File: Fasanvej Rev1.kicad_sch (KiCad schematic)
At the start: 43 parts

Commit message: Finalized schematics some more. Still missing a few footprints.
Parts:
- removed J?: AudioJack3, Connector_Audio:Jack_3.5mm_CUI_SJ-3523-SMT_Horizontal, symbol Connector:AudioJack3
- removed J?: USB_A, symbol Connector:USB_A
- removed LS?: Soberton SP-1609-2, Connector_PinHeader_2.54mm:PinHeader_1x02_P2.54mm_Vertical, symbol Device:Speaker
- removed RV?: 1k, symbol Device:R_Potentiometer_Dual
- removed SW?: SW_DPDT_x2, symbol Switch:SW_DPDT_x2
- removed SW?: SW_DPDT_x2, Button_Switch_THT:SW_E-Switch_EG2219_DPDT_Angled, symbol Switch:SW_DPDT_x2
- added FID1, FID2: Fiducial, Fiducial:Fiducial_1.5mm_Mask3mm, symbol Mechanical:Fiducial
- added H1, H2, H3, H4, H5, H6, H7, H8: M3, MountingHole:MountingHole_3.2mm_M3, symbol Mechanical:MountingHole
- added J1, J2: Molex 676430910, RISRES Library:USB_A_Molex_67643_Horizontal, symbol Connector:USB_A
- added J5: UART console, Connector_PinHeader_2.54mm:PinHeader_1x04_P2.54mm_Vertical, symbol Connector_Generic:Conn_01x04
- J3: renamed from J?; footprint (none) -> RISRES Library:TE_4-1734839-0_1x40-1MP_P0.5mm_Horizontal
- SW1: renamed from SW?; value SW_Push -> TL3342F260QG; footprint (none) -> Button_Switch_SMD:SW_SPST_TL3342
- Y1: renamed from Y?; footprint (none) -> Crystal:Crystal_SMD_HC49-SD_HandSoldering
- gave numbers to parts that had none: 34
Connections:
- net SPK_LEFT is gone; now on net HP_L: LS1.2
- net +3V3: now also J5.1 (Pin_1)
- net GND: now also J1.4 (GND), J1.5 (Shield), J2.4 (GND), J5.4 (Pin_4)
- net UART_RX: now also J5.2 (Pin_2)
- net UART_TX: now also J5.3 (Pin_3)
- net USB_DM_WIFI: now also J1.2 (D-)
- net USB_DP_WIFI: now also J1.3 (D+)
- net USB_VBUS_EXTERNAL: now also J2.1 (VBUS)
- net at C4.2, R4.1, U2.2 (GND): now also J2.5 (Shield)
- net at U2.4 (I/O2): now also J2.3 (D+)
- net at U2.6 (I/O1): now also J2.2 (D-)
- new net +5V: J1.1 (VBUS)
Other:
- moved on the sheet: C10, C11, C12, C13, C14, C15, C16, C17, C18, C7, C8, C9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

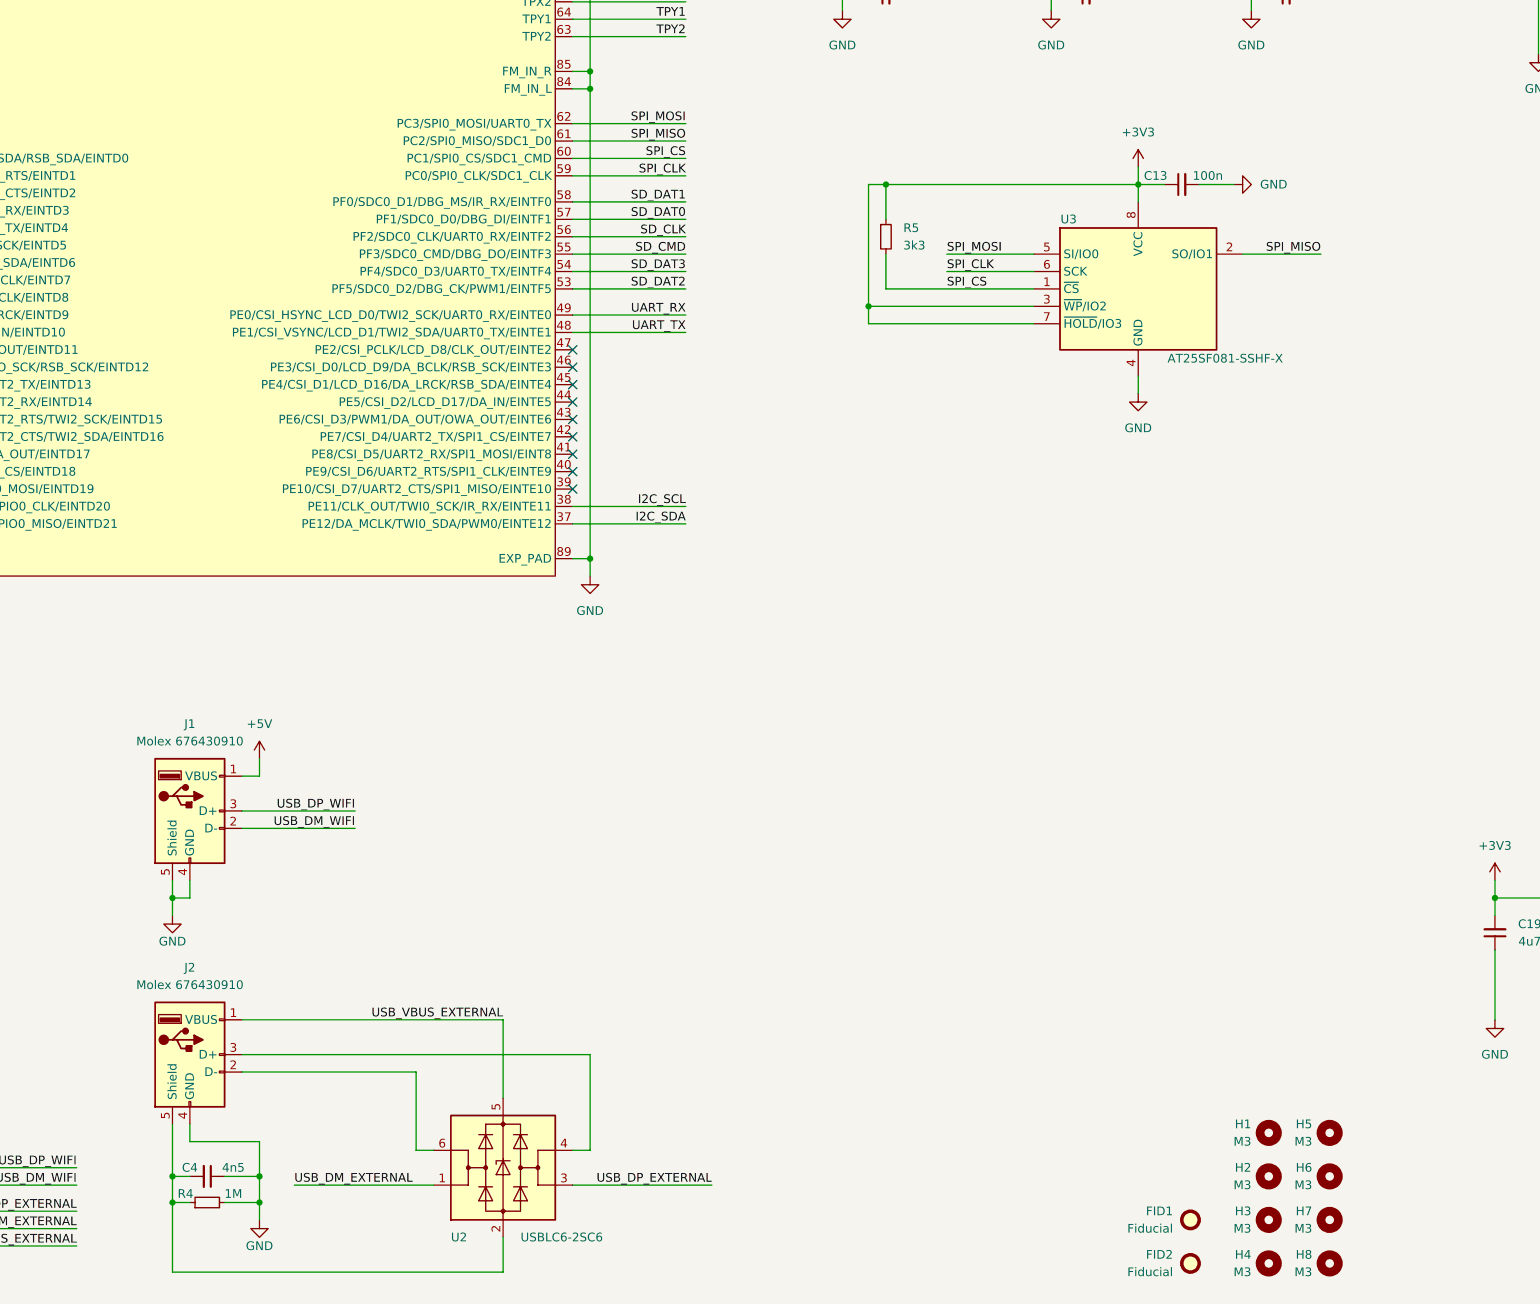
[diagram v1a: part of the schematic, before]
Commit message: Schematic finalized. Started PCB layout.
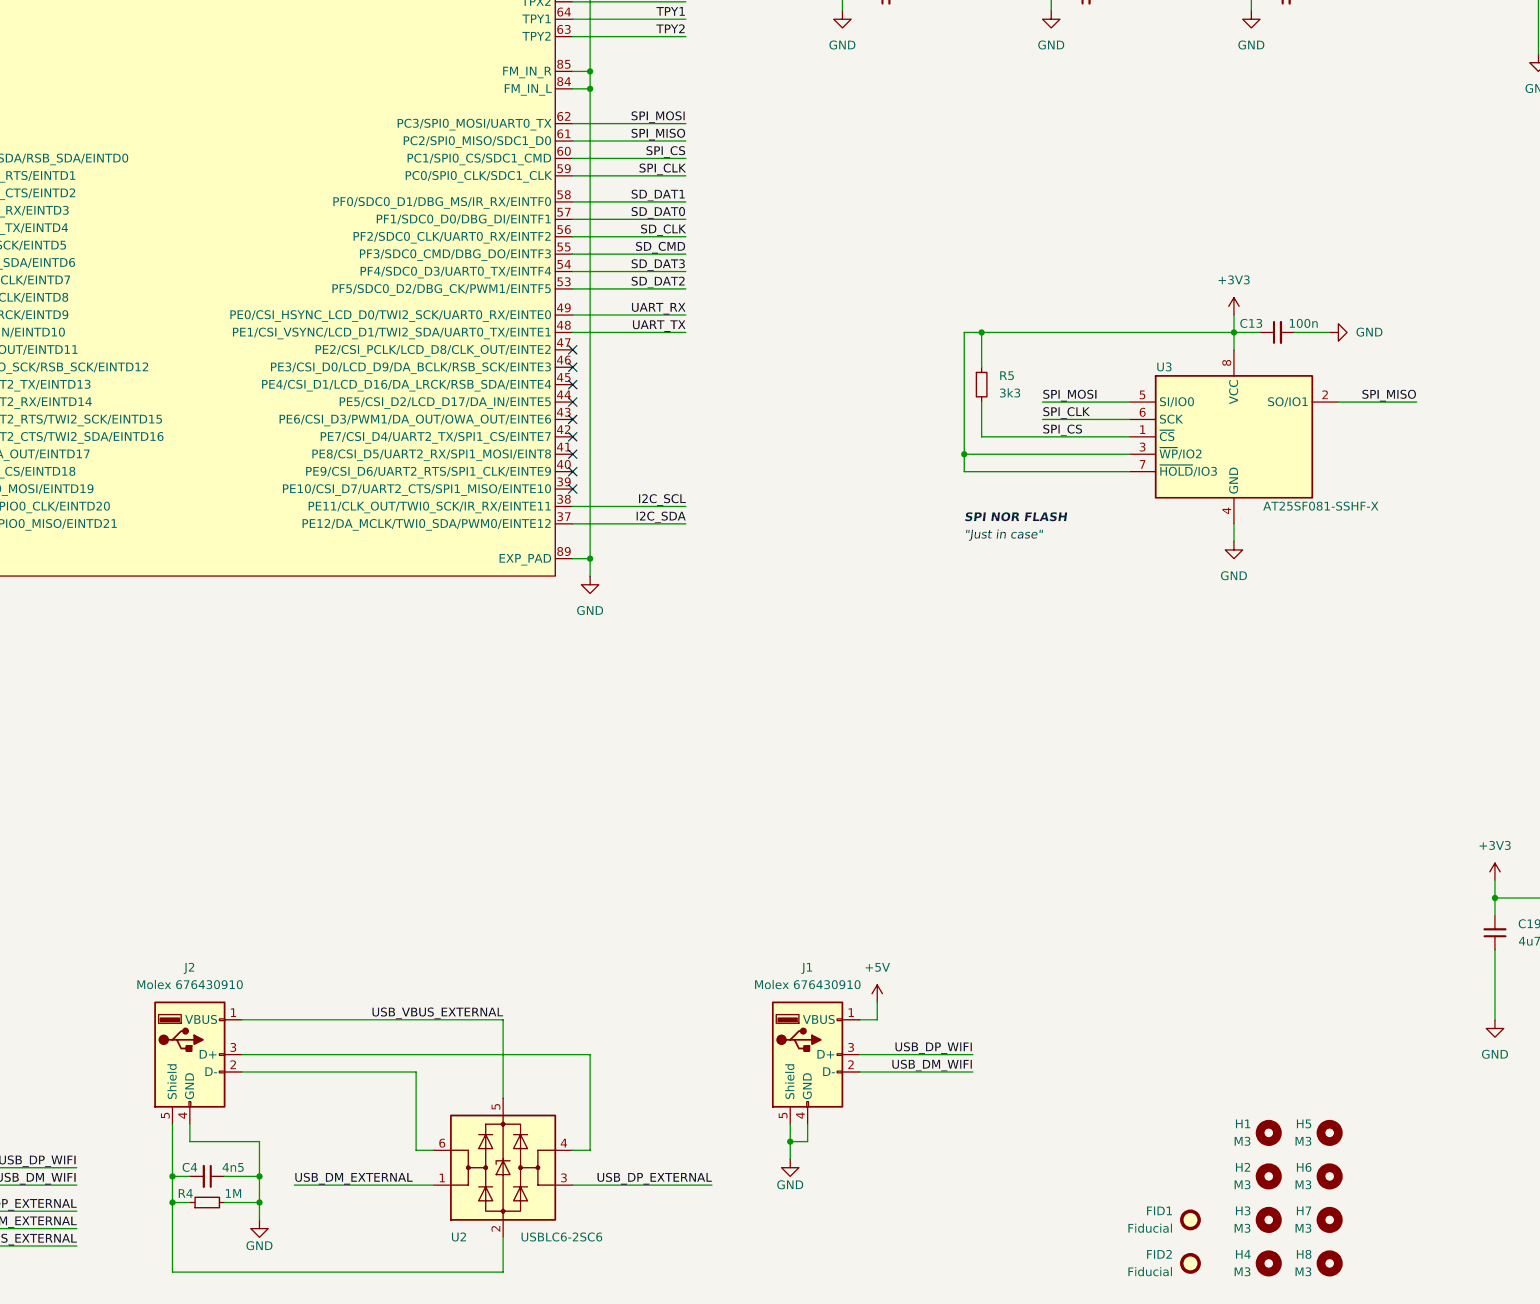
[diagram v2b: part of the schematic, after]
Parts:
- J4: footprint (none) -> Connector_Card:microSD_HC_Hirose_DM3D-SF
- U1: footprint (none) -> RISRES Library:QFN-88_EP_10x10_Pitch0.4mm
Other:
- note added: ""Just in case""
- note added: "SPI NOR FLASH"
- moved on the sheet: C13, J1, R5, U3

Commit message: Made a lot of progress laying out PCB
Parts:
- removed J3: LCD_RGB_40P, RISRES Library:TE_4-1734839-0_1x40-1MP_P0.5mm_Horizontal, symbol RISRES Library:LCD_RGB_40P
- removed TP2, TP3: TestPoint_Small, TestPoint:TestPoint_Pad_D4.0mm, symbol Connector:TestPoint_Small
- added J13: I2C keyboard, Connector_PinHeader_2.54mm:PinHeader_2x02_P2.54mm_Vertical, symbol Connector_Generic:Conn_02x02_Top_Bottom
- added J3: LQ035NC111, RISRES Library:FFC2B22-54-T, symbol Connector_Generic:Conn_02x27_Counter_Clockwise
- added R43, R44: 4k7, Resistor_SMD:R_0603_1608Metric_Pad0.98x0.95mm_HandSolder, symbol Device:R_Small
- added R45: 22k, Resistor_SMD:R_0603_1608Metric_Pad0.98x0.95mm_HandSolder, symbol Device:R_Small
- renumbered J2 to J1, J1 to J2
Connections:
- net +3V3: now also J3.41 (Pin_41), J3.42 (Pin_42), R43.1, R44.1, R45.2
- net GND: now also J3.12 (Pin_12), J3.13 (Pin_13), J3.20 (Pin_20), J3.21 (Pin_21), J3.28 (Pin_28), J3.29 (Pin_29), J3.48 (Pin_48), J3.49 (Pin_49), J3.50 (Pin_50), J3.53 (Pin_53), J3.54 (Pin_54)
- net I2C_SCL: now also J13.1 (Pin_1), R43.2; no longer TP1.1
- net I2C_SDA: now also J13.2 (Pin_2), R44.2
- net LCD_CLK: now also J3.38 (Pin_38)
- net LCD_D10: now also J3.22 (Pin_22)
- net LCD_D11: now also TP1.1, J3.23 (Pin_23)
- net LCD_D12: now also J3.24 (Pin_24)
- net LCD_D13: now also J3.25 (Pin_25)
- net LCD_D14: now also J3.26 (Pin_26)
- net LCD_D15: now also J3.27 (Pin_27)
- net LCD_D18: now also J3.35 (Pin_35)
- net LCD_D19: now also J3.34 (Pin_34)
- net LCD_D2: now also J3.14 (Pin_14)
- net LCD_D20: now also J3.33 (Pin_33)
- net LCD_D21: now also J3.32 (Pin_32)
- net LCD_D22: now also J3.31 (Pin_31)
- net LCD_D23: now also J3.30 (Pin_30)
- net LCD_D3: now also J3.15 (Pin_15)
- net LCD_D4: now also J3.16 (Pin_16)
- net LCD_D5: now also J3.17 (Pin_17)
- net LCD_D6: now also J3.18 (Pin_18)
- net LCD_D7: now also J3.19 (Pin_19)
- net LCD_DE: now also J3.52 (Pin_52)
- net LCD_HSYNC: now also J3.36 (Pin_36)
- net LCD_VSYNC: now also J3.37 (Pin_37)
- net LED_BACKLIGHT_A: now also J3.3 (Pin_3), J3.4 (Pin_4)
- net LED_BACKLIGHT_K: now also J3.1 (Pin_1), J3.2 (Pin_2)
- net USB_DM_EXTERNAL: now also U2.3 (I/O2); no longer U2.1 (I/O1)
- net USB_DP_EXTERNAL: now also U2.1 (I/O1); no longer U2.3 (I/O2)
- net at J1.2 (D-): now also U2.4 (I/O2); no longer U2.6 (I/O1)
- net at J1.3 (D+): now also U2.6 (I/O1); no longer U2.4 (I/O2)
- new net: J3.10 (Pin_10), J3.11 (Pin_11), J3.8 (Pin_8), J3.9 (Pin_9), R45.1
- new net KEYBOARD_S1_P0: J13.3 (Pin_3)
- new net KEYBOARD_S1_P1: J13.4 (Pin_4)
- no-connect marks 17 -> 28
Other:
- sheet Keyboard ports: added SERCOM1_PAD0, SERCOM1_PAD1; removed none
- moved on the sheet: C21, TP1

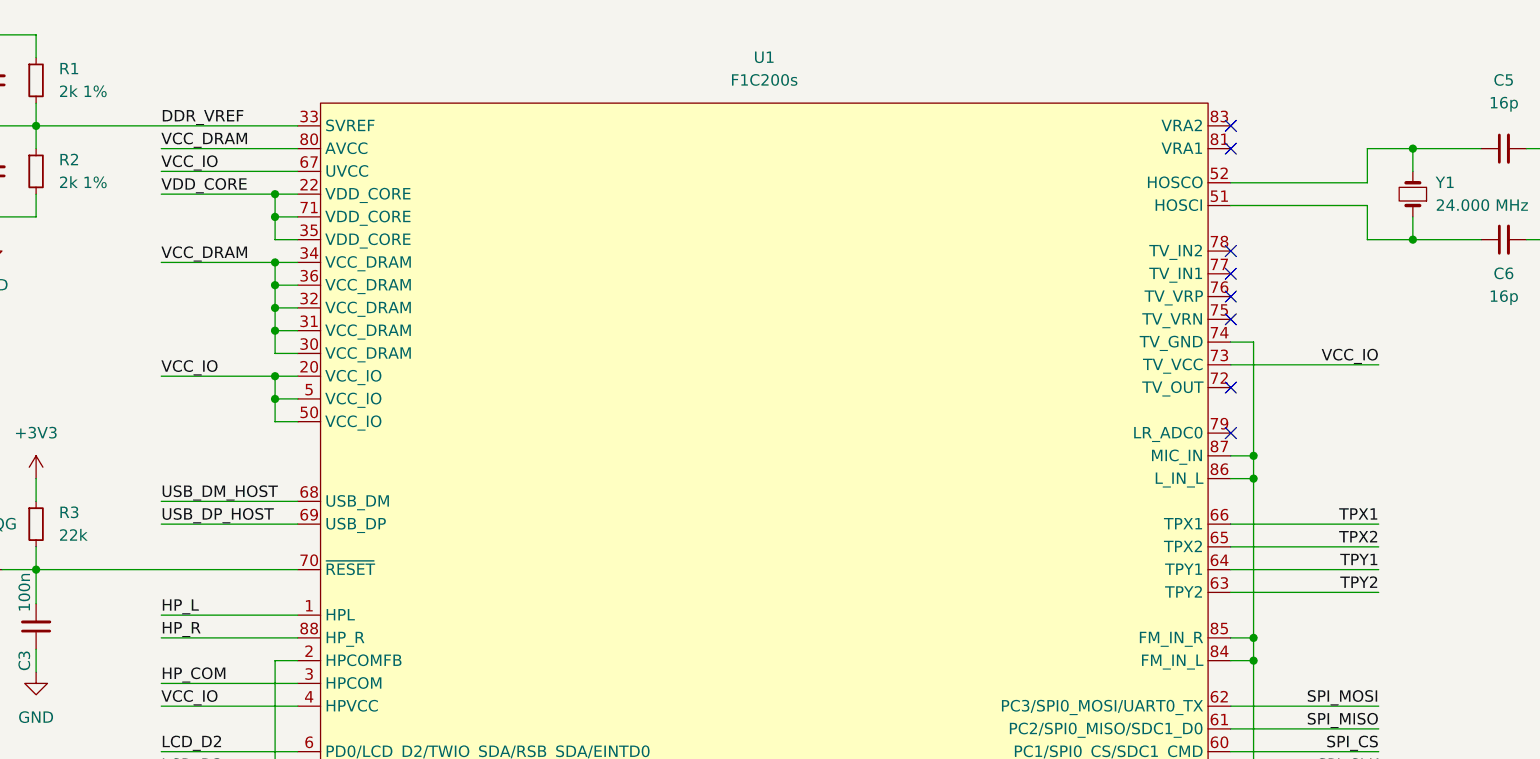
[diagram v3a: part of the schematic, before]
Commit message: Made progress with board layout as well as mechanical (case) design
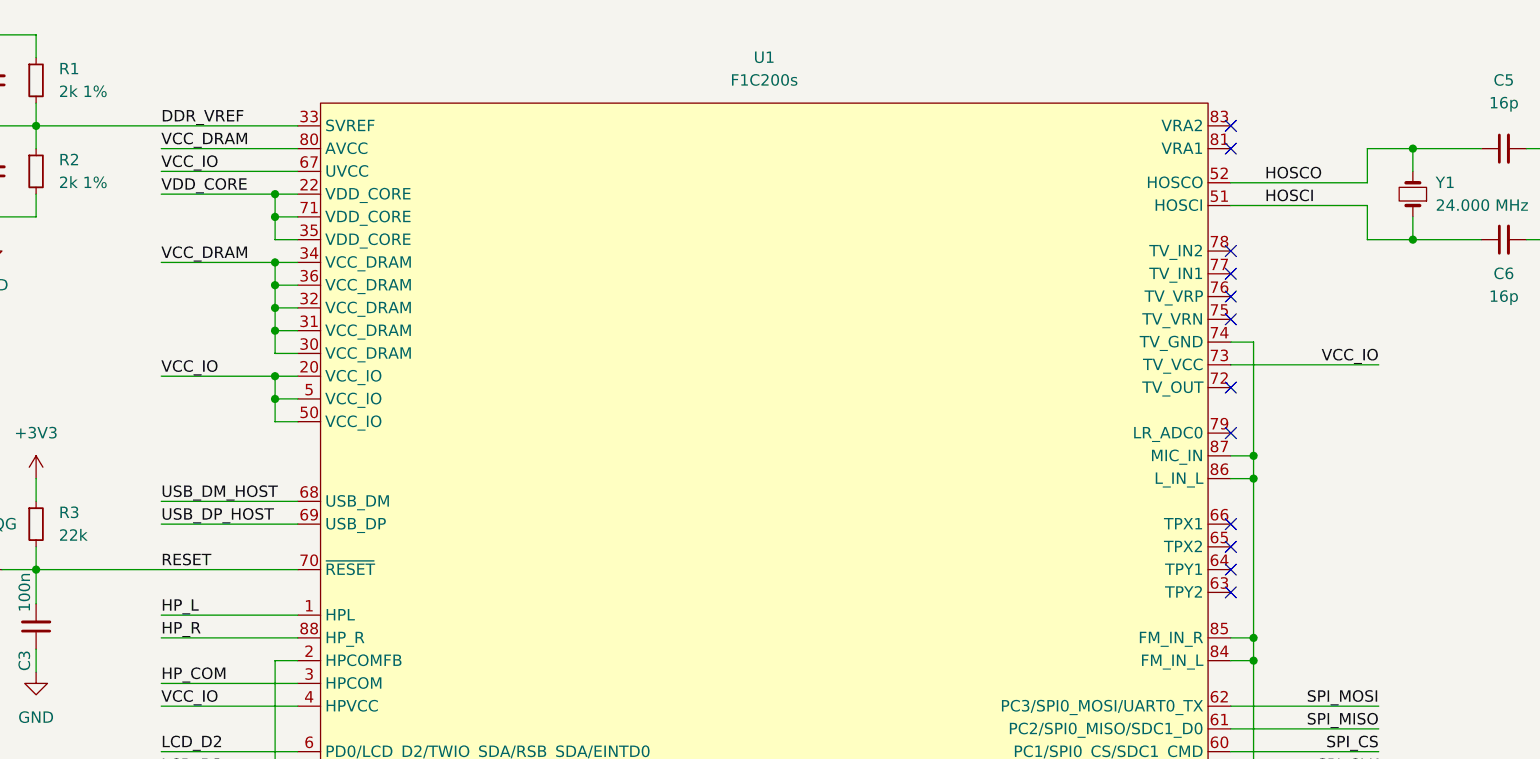
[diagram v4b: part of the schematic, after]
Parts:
- TP1: footprint TestPoint:TestPoint_Pad_D4.0mm -> TestPoint:TestPoint_Pad_D2.5mm
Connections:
- net HOSCI: now reaches C6.1, U1.51 (HOSCI), Y1.1
- net HOSCO: now reaches C5.1, U1.52 (HOSCO), Y1.2
- net RESET: now reaches C3.2, R3.2, SW1.2, U1.70 (~{RESET})
- net TPX1: no longer names the net of U1.66 (TPX1)
- net TPX2: no longer names the net of U1.65 (TPX2)
- net TPY1: no longer names the net of U1.64 (TPY1)
- net TPY2: no longer names the net of U1.63 (TPY2)
- no-connect marks 28 -> 32
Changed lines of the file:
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@@
   (no_connect (at 181.61 44.45))
   (no_connect (at 181.61 46.99))
+  (no_connect (at 181.61 96.52))
+  (no_connect (at 181.61 88.9))
+  (no_connect (at 181.61 91.44))
+  (no_connect (at 181.61 93.98))
   (wire (pts (xy 184.15 259.08) (xy 181.61 259.08))
     (stroke (width 0) (type default) (color 0 0 0 0))
@@
     (stroke (width 0) (type default) (color 0 0 0 0))
   )
-  (wire (pts (xy 181.61 93.98) (xy 198.12 93.98))
-    (stroke (width 0) (type default) (color 0 0 0 0))
-  )
   (wire (pts (xy 288.29 90.17) (xy 293.37 90.17))
     (stroke (width 0) (type default) (color 0 0 0 0))
@@
     (stroke (width 0) (type default) (color 0 0 0 0))
   )
-  (wire (pts (xy 181.61 91.44) (xy 198.12 91.44))
-    (stroke (width 0) (type default) (color 0 0 0 0))
-  )
   (wire (pts (xy 241.3 149.86) (xy 241.3 154.94))
     (stroke (width 0) (type default) (color 0 0 0 0))
@@
     (stroke (width 0) (type default) (color 0 0 0 0))
   )
-  (wire (pts (xy 181.61 96.52) (xy 198.12 96.52))
-    (stroke (width 0) (type default) (color 0 0 0 0))
-  )
   (wire (pts (xy 356.87 78.74) (xy 373.38 78.74))
     (stroke (width 0) (type default) (color 0 0 0 0))
@@
     (stroke (width 0) (type default) (color 0 0 0 0))
   )
-  (wire (pts (xy 181.61 88.9) (xy 198.12 88.9))
-    (stroke (width 0) (type default) (color 0 0 0 0))
-  )
   (wire (pts (xy 229.87 90.17) (xy 234.95 90.17))
     (stroke (width 0) (type default) (color 0 0 0 0))
@@
     (effects (font (size 1.27 1.27)) (justify right bottom))
   )
+  (label "HOSCO" (at 185.42 50.8 0)
+    (effects (font (size 1.27 1.27)) (justify left bottom))
+  )
   (label "LCD_D22" (at 373.38 86.36 180)
     (effects (font (size 1.27 1.27)) (justify right bottom))
@@
     (effects (font (size 1.27 1.27)) (justify left bottom))
   )
-  (label "TPY1" (at 198.12 93.98 180)
-    (effects (font (size 1.27 1.27)) (justify right bottom))
-  )
   (label "VCC_DRAM" (at 62.23 46.99 0)
     (effects (font (size 1.27 1.27)) (justify left bottom))
@@
     (effects (font (size 1.27 1.27)) (justify right bottom))
   )
+  (label "RESET" (at 62.23 93.98 0)
+    (effects (font (size 1.27 1.27)) (justify left bottom))
+  )
   (label "I2C_SDA" (at 334.01 128.27 0)
     (effects (font (size 1.27 1.27)) (justify left bottom))
@@
     (effects (font (size 1.27 1.27)) (justify left bottom))
   )
-  (label "TPY2" (at 198.12 96.52 180)
-    (effects (font (size 1.27 1.27)) (justify right bottom))
-  )
   (label "VCC_DRAM" (at 275.59 85.09 180)
     (effects (font (size 1.27 1.27)) (justify right bottom))
   )
+  (label "HOSCI" (at 185.42 53.34 0)
+    (effects (font (size 1.27 1.27)) (justify left bottom))
+  )
   (label "SPI_MISO" (at 304.8 149.86 180)
     (effects (font (size 1.27 1.27)) (justify right bottom))
@@
     (effects (font (size 1.27 1.27)) (justify left bottom))
   )
-  (label "TPX2" (at 198.12 91.44 180)
-    (effects (font (size 1.27 1.27)) (justify right bottom))
-  )
   (label "SD_DAT3" (at 337.82 217.17 0)
     (effects (font (size 1.27 1.27)) (justify left bottom))
@@
     (effects (font (size 1.27 1.27)) (justify right bottom))
   )
-  (label "TPX1" (at 198.12 88.9 180)
-    (effects (font (size 1.27 1.27)) (justify right bottom))
-  )
   (label "KEYBOARD_S1_P1" (at 394.97 128.27 180)
     (effects (font (size 1.27 1.27)) (justify right bottom))
@@
       (effects (font (size 1.27 1.27)) (justify left) hide)
     )
-    (property "Footprint" "TestPoint:TestPoint_Pad_D4.0mm" (id 2) (at 383.54 195.58 0)
+    (property "Footprint" "TestPoint:TestPoint_Pad_D2.5mm" (id 2) (at 383.54 195.58 0)
       (effects (font (size 1.27 1.27)) hide)
     )
@@
     )
     (path "/0c4582c9-586c-41ef-9e83-201c08570f6d"
-      (reference "TP1") (unit 1) (value "TestPoint_Small") (footprint "TestPoint:TestPoint_Pad_D4.0mm")
+      (reference "TP1") (unit 1) (value "TestPoint_Small") (footprint "TestPoint:TestPoint_Pad_D2.5mm")
     )
     (path "/12439ab1-001a-4ff9-885e-cb05f91099cb"
